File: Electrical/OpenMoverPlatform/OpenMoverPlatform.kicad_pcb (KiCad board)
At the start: 2 copper layers, 95 x 72.5 mm, 32 parts, among them J1 battery supply, J2 BLDC1 POWER, J3 BLDC2 POWER, J4 GPS_MAG, J5 I2C_1, J6 BLDC1 PWM, J7 BLDC2 PWM, J8 I2C_2, J9 MOD_SERIAL, U1 WeMos_LoLin32_Lite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

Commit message: ki cad pcb update
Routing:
- net Net-(J3-Pin_2): track 48.9 -> 51.1 mm
- net IO4_RXMOD: track 107.5 -> 107.8 mm, vias 1 -> 2
- net IO5_TXMOD: track 114.9 -> 115.0 mm, vias 1 -> 2
- net IO12_PWM1: track 128.6 -> 128.7 mm, vias 1 -> 2
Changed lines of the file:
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@@
 	)
 	(segment
-		(start 203.73264 53.11)
+		(start 173 52)
+		(end 176.75 55.75)
+		(width 3)
+		(layer "B.Cu")
+		(net 4)
+	)
+	(segment
+		(start 170.22 52)
+		(end 173 52)
+		(width 3)
+		(layer "B.Cu")
+		(net 4)
+	)
+	(segment
+		(start 169.92 48.9)
+		(end 169.92 52.3)
+		(width 3)
+		(layer "B.Cu")
+		(net 4)
+	)
+	(segment
+		(start 208.6 48.24264)
+		(end 208.6 44)
+		(width 3)
+		(layer "B.Cu")
+		(net 4)
+	)
+	(segment
+		(start 201.09264 55.75)
 		(end 208.6 48.24264)
+		(width 3)
+		(layer "B.Cu")
+		(net 4)
+	)
+	(segment
+		(start 176.75 55.75)
+		(end 201.09264 55.75)
 		(width 3)
 		(layer "B.Cu")
@@
 	)
 	(segment
-		(start 170.22 52)
-		(end 176.453095 52)
-		(width 3)
-		(layer "B.Cu")
-		(net 4)
-	)
-	(segment
-		(start 169.92 48.9)
-		(end 169.92 52.3)
-		(width 3)
-		(layer "B.Cu")
-		(net 4)
-	)
-	(segment
-		(start 177.563095 53.11)
-		(end 203.73264 53.11)
-		(width 3)
-		(layer "B.Cu")
-		(net 4)
-	)
-	(segment
-		(start 176.453095 52)
-		(end 177.563095 53.11)
-		(width 3)
-		(layer "B.Cu")
-		(net 4)
-	)
-	(segment
-		(start 208.6 48.24264)
-		(end 208.6 44)
-		(width 3)
-		(layer "B.Cu")
-		(net 4)
-	)
-	(segment
 		(start 174 64)
 		(end 172.5 62.5)
@@
 	)
 	(segment
+		(start 177.42 92.08)
+		(end 178.2 91.3)
+		(width 1)
+		(layer "B.Cu")
+		(net 11)
+	)
+	(segment
 		(start 182 87.24)
 		(end 187.5 87.24)
@@
 	)
 	(segment
+		(start 147.9995 68.0005)
+		(end 153.43 68.0005)
+		(width 1)
+		(layer "B.Cu")
+		(net 11)
+	)
+	(segment
+		(start 145.1 70.9)
+		(end 147.9995 68.0005)
+		(width 1)
+		(layer "B.Cu")
+		(net 11)
+	)
+	(segment
 		(start 178.2 89.837919)
 		(end 180.797919 87.24)
@@
 	)
 	(segment
-		(start 147.9995 68.0005)
-		(end 153.43 68.0005)
-		(width 1)
-		(layer "B.Cu")
-		(net 11)
-	)
-	(segment
-		(start 145.1 70.9)
-		(end 147.9995 68.0005)
-		(width 1)
-		(layer "B.Cu")
-		(net 11)
-	)
-	(segment
-		(start 178.2 91.8)
-		(end 178.2 89.837919)
-		(width 1)
-		(layer "B.Cu")
-		(net 11)
-	)
-	(segment
-		(start 177.92 92.08)
-		(end 178.2 91.8)
-		(width 1)
-		(layer "B.Cu")
-		(net 11)
-	)
-	(segment
-		(start 175.5 92.08)
-		(end 177.92 92.08)
-		(width 1)
-		(layer "B.Cu")
-		(net 11)
-	)
-	(segment
 		(start 145.1 94.423044)
 		(end 145.1 70.9)
@@
 	)
 	(segment
+		(start 178.2 91.3)
+		(end 178.2 89.837919)
+		(width 1)
+		(layer "B.Cu")
+		(net 11)
+	)
+	(segment
+		(start 175.5 92.08)
+		(end 177.42 92.08)
+		(width 1)
+		(layer "B.Cu")
+		(net 11)
+	)
+	(segment
 		(start 149.115434 96.6)
 		(end 146.4 93.884566)
@@
 	)
 	(segment
-		(start 133.7195 85.7805)
-		(end 130.57 85.7805)
-		(width 1)
-		(layer "F.Cu")
-		(net 13)
-	)
-	(segment
 		(start 138 48)
 		(end 134.7 51.3)
@@
 	(segment
 		(start 134.7 84.8)
-		(end 133.7195 85.7805)
+		(end 133.75 85.75)
 		(width 1)
 		(layer "F.Cu")
@@
 	)
 	(segment
+		(start 133.75 85.75)
+		(end 133.7195 85.7805)
+		(width 1)
+		(layer "F.Cu")
+		(net 13)
+	)
+	(segment
 		(start 208.5 32)
 		(end 146.5 32)
@@
 		(net 13)
 	)
+	(via
+		(at 133.75 85.75)
+		(size 1.5)
+		(drill 1)
+		(layers "F.Cu" "B.Cu")
+		(net 13)
+	)
 	(segment
 		(start 209.42 33)
@@
 	)
 	(segment
+		(start 133.75 85.75)
+		(end 130.6005 85.75)
+		(width 1)
+		(layer "B.Cu")
+		(net 13)
+	)
+	(segment
+		(start 130.6005 85.75)
+		(end 130.57 85.7805)
+		(width 1)
+		(layer "B.Cu")
+		(net 13)
+	)
+	(segment
 		(start 211.42 35)
 		(end 209.5 33.08)
@@
 	)
 	(segment
+		(start 143.9595 70.5405)
+		(end 150 70.5)
+		(width 1)
+		(layer "F.Cu")
+		(net 17)
+	)
+	(segment
 		(start 190.5 89.5)
 		(end 190.5 80)
@@
 	)
 	(segment
-		(start 143.9595 70.5405)
-		(end 153.43 70.5405)
-		(width 1)
-		(layer "F.Cu")
-		(net 17)
-	)
-	(segment
 		(start 137.3 86.3)
 		(end 137.3 77.2)
@@
 	)
 	(segment
+		(start 150 70.5)
+		(end 149.9595 70.5405)
+		(width 1)
+		(layer "F.Cu")
+		(net 17)
+	)
+	(segment
 		(start 189 78.5)
 		(end 174.5 78.5)
@@
 	)
 	(via
+		(at 150 70.5)
+		(size 1.5)
+		(drill 1)
+		(layers "F.Cu" "B.Cu")
+		(net 17)
+	)
+	(via
 		(at 190.5 89.5)
 		(size 1.5)
 		(drill 1)
 		(layers "F.Cu" "B.Cu")
+		(net 17)
+	)
+	(segment
+		(start 150.0405 70.5405)
+		(end 150 70.5)
+		(width 1)
+		(layer "B.Cu")
+		(net 17)
+	)
+	(segment
+		(start 153.43 70.5405)
+		(end 150.0405 70.5405)
+		(width 1)
+		(layer "B.Cu")
 		(net 17)
 	)
@@
 	)
 	(segment
-		(start 139.8395 78.1605)
-		(end 153.43 78.1605)
+		(start 140.25 77.75)
+		(end 150 77.75)
 		(width 1)
 		(layer "F.Cu")
@@
 	)
 	(segment
+		(start 139.8395 78.1605)
+		(end 140.25 77.75)
+		(width 1)
+		(layer "F.Cu")
+		(net 18)
+	)
+	(segment
 		(start 138.6 85.761522)
 		(end 138.6 79.4)
@@
 	)
 	(via
+		(at 150 77.75)
+		(size 1.5)
+		(drill 1)
+		(layers "F.Cu" "B.Cu")
+		(net 18)
+	)
+	(via
 		(at 192.5 90.5)
 		(size 1.5)
 		(drill 1)
 		(layers "F.Cu" "B.Cu")
+		(net 18)
+	)
+	(segment
+		(start 153.43 78.1605)
+		(end 150.4105 78.1605)
+		(width 1)
+		(layer "B.Cu")
 		(net 18)
 	)
@@
 		(width 1)
 		(layer "B.Cu")
+		(net 18)
+	)
+	(segment
+		(start 150.4105 78.1605)
+		(end 150 77.75)
+		(width 1)
+		(layer "B.Cu")

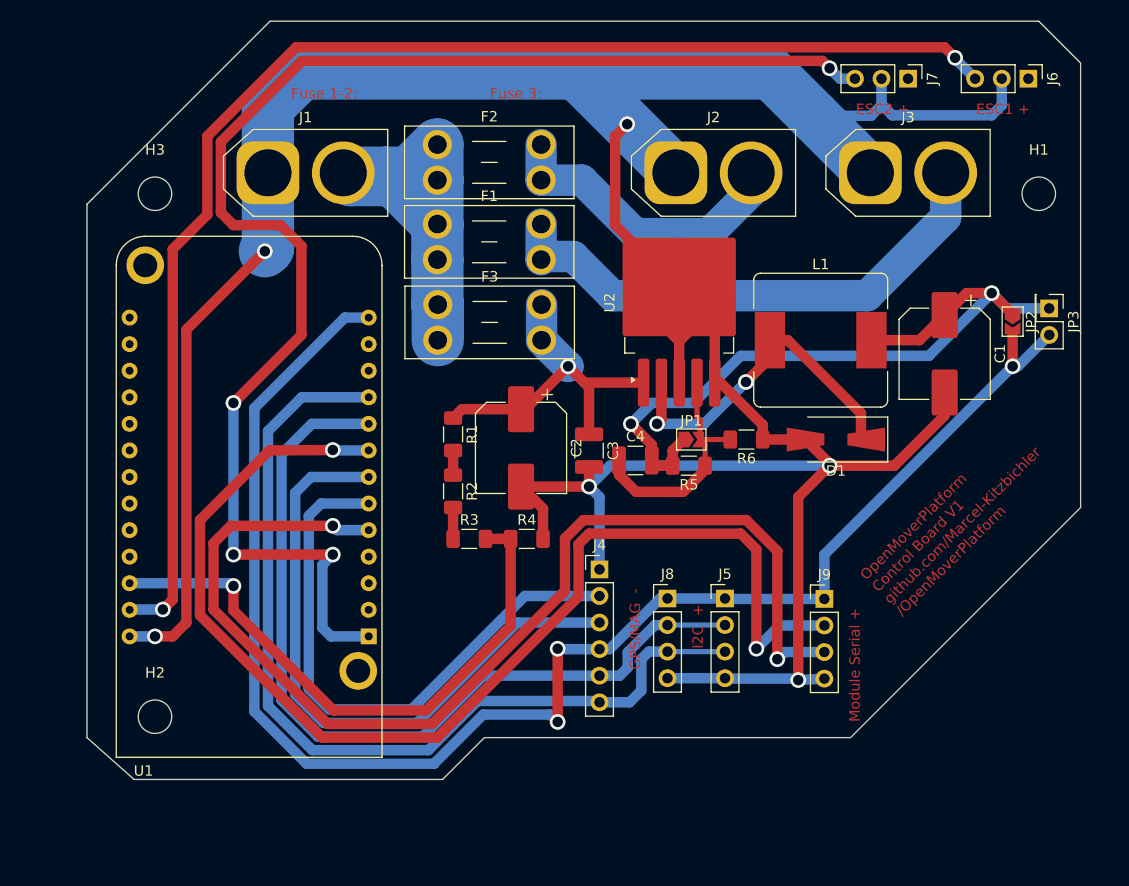
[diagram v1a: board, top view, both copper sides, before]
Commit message: updated pcb to use esp32 s3 wroom 1
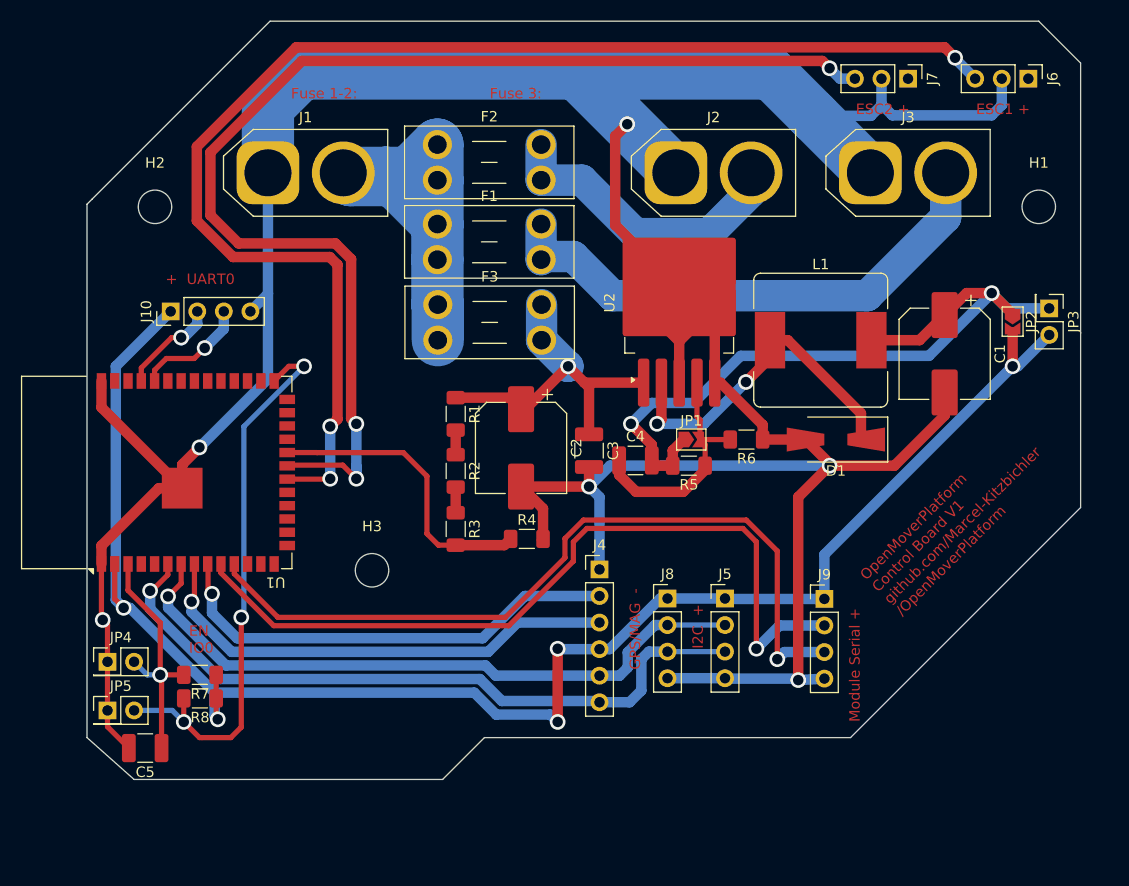
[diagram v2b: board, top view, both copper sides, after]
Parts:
- added C5: C, Capacitor_SMD:C_1210_3225Metric_Pad1.33x2.70mm_HandSolder, F.Cu at (132.1, 99.0)
- added J10: SERIAL0, Connector_PinHeader_2.54mm:PinHeader_1x04_P2.54mm_Vertical, F.Cu at (134.5, 57.2)
- added JP4: Reset, Connector_PinHeader_2.54mm:PinHeader_2x01_P2.54mm_Vertical, F.Cu at (128.5, 90.8)
- added JP5: Boot, Connector_PinHeader_2.54mm:PinHeader_2x01_P2.54mm_Vertical, F.Cu at (128.5, 95.4)
- added R7: R, Resistor_SMD:R_1206_3216Metric_Pad1.30x1.75mm_HandSolder, F.Cu at (137.3, 92.0)
- added R8: R, Resistor_SMD:R_1206_3216Metric_Pad1.30x1.75mm_HandSolder, F.Cu at (137.3, 94.2)
- U1: value WeMos_LoLin32_Lite -> ESP32-S3-WROOM-1; footprint customFootprints:lolin32lite -> RF_Module:ESP32-S3-WROOM-1
- moved H2 48.8 mm to (133.0, 47.2)
- moved H3 41.6 mm to (153.8, 82.0)
- moved U1 25.6 mm to (133.1, 72.7), turned to 90 degrees
- moved R1 1.97 mm to (161.8, 67.0)
- moved R2 1.97 mm to (161.8, 72.5)
- moved R3 1.61 mm to (161.8, 78.0), turned to -90 degrees
- moved H1 1.25 mm to (217.5, 47.2)
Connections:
- J4 pad 3: IO17_TXGPS -> IO15_TXGPS
- J4 pad 5: IO18_SDA -> IO7_SDA
- J4 pad 6: IO23_SCL -> IO6_SCL
- J5 pad 2: IO18_SDA -> IO7_SDA
- J5 pad 3: IO23_SCL -> IO6_SCL
- J8 pad 2: IO18_SDA -> IO7_SDA
- J8 pad 3: IO23_SCL -> IO6_SCL
- J9 pad 2: IO5_TXMOD -> IO17_TXMOD
- J9 pad 3: IO4_RXMOD -> IO18_RXMOD
- U1 pad 1: IO13_PWM2 -> GND
- U1 pad 10: IO23_SCL -> IO17_TXMOD
- U1 pad 11: unconnected-(U1-GPIO19-Pad11) -> IO18_RXMOD
- U1 pad 13: +3V3 -> IO19_D-
- U1 pad 14: unconnected-(U1-GPIO36-Pad14) -> IO20_D+
- U1 pad 2: unconnected-(U1-GPIO15-Pad2) -> +3V3
- U1 pad 20: unconnected-(U1-GPIO33-Pad20) -> IO12_PWM1
- U1 pad 21: unconnected-(U1-GPIO25-Pad21) -> IO13_PWM2
- U1 pad 22: unconnected-(U1-GPIO26-Pad22) -> IO14_BatADC
- U1 pad 24: IO14_BatADC -> unconnected-(U1-IO47-Pad24)
- U1 pad 25: IO12_PWM1 -> unconnected-(U1-IO48-Pad25)
- U1 pad 26: GND -> unconnected-(U1-IO45-Pad26)
- U1 pad 3: unconnected-(U1-GPIO02-Pad3) -> EN
- U1 pad 5: IO4_RXMOD -> unconnected-(U1-IO5-Pad5)
- U1 pad 6: IO16_RXGPS -> IO6_SCL
- U1 pad 7: IO17_TXGPS -> IO7_SDA
- U1 pad 8: IO5_TXMOD -> IO15_TXGPS
- U1 pad 9: IO18_SDA -> IO16_RXGPS
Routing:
- net IO5_TXMOD: track 115.0 -> 0.00 mm, vias 2 -> 0
- net IO4_RXMOD: track 107.8 -> 0.00 mm, vias 2 -> 0
- net IO23_SCL: track 88.4 -> 0.00 mm
- net IO18_SDA: track 82.2 -> 0.00 mm
- net IO17_TXMOD: track 0.00 -> 77.6 mm, vias 0 -> 1
- net IO18_RXMOD: track 0.00 -> 75.9 mm, vias 0 -> 1
- net IO6_SCL: track 0.00 -> 67.5 mm, vias 0 -> 1
- net IO7_SDA: track 0.00 -> 63.5 mm, vias 0 -> 1
- net IO17_TXGPS: track 61.1 -> 0.00 mm
- net IO0: track 0.00 -> 54.8 mm, vias 0 -> 3
- net IO15_TXGPS: track 0.00 -> 46.4 mm, vias 0 -> 1
- net IO14_BatADC: track 56.9 -> 28.5 mm, vias 1 -> 0
- net GND: track 306.8 -> 334.4 mm
- net EN: track 0.00 -> 24.2 mm, vias 0 -> 1
- net IO13_PWM2: track 134.2 -> 116.8 mm, vias 4 -> 3
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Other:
- board text added: "+ UART0"
- board text added: "EN IO0"

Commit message: update 2025
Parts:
- added C6: C, Capacitor_SMD:C_1210_3225Metric_Pad1.33x2.70mm_HandSolder, F.Cu at (129.3, 57.2)
- added J11: USB_B, Connector_USB:USB_B_OST_USB-B1HSxx_Horizontal, F.Cu at (152.6, 95.0)
- F1, F2, F3: footprint Fuse:Fuseholder_Blade_Mini_Keystone_3568 -> Fuse:Fuse_Blade_Mini_directSolder
- moved H3 3.75 mm to (153.8, 78.2)
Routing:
- net GND: track 334.4 -> 374.3 mm
- net IO20_D+: track 0.00 -> 22.6 mm, vias 0 -> 1
- net IO19_D-: track 0.00 -> 20.2 mm, vias 0 -> 1
- net +3V3: track 160.8 -> 165.2 mm, vias 5 -> 6
- net Net-(J1-Pin_2): track 45.2 -> 41.8 mm
- net IO0: track 54.8 -> 56.5 mm
- net IO16_RXGPS: track 44.6 -> 43.3 mm
- net IO17_TXMOD: track 77.6 -> 76.6 mm, vias 1 -> 3
- net IO15_TXGPS: track 46.4 -> 45.5 mm
- net +BATT: track 32.9 -> 33.7 mm
- net IO18_RXMOD: track 75.9 -> 75.3 mm, vias 1 -> 3
